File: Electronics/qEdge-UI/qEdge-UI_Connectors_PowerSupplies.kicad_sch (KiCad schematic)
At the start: 29 parts, among them IC201 NCP1117ST33T3G, IC202 AP64501SP-13, J201 Conn_01x02_Male, J202 Conn_01x03_Male

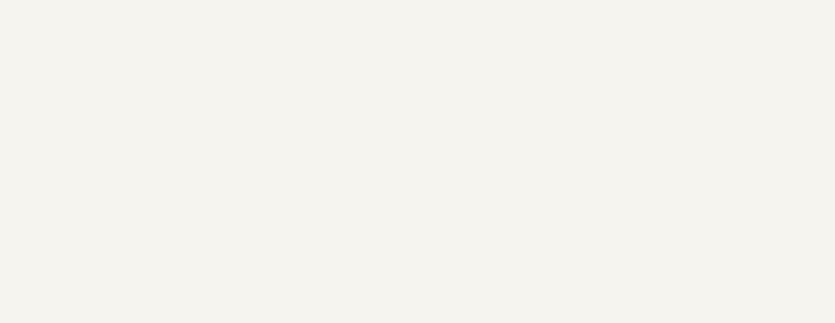
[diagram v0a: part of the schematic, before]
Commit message: added READMEs for Mechanic and Electronic added License in the Electronic schematics restructured Mechanics for better readability and reproducibility
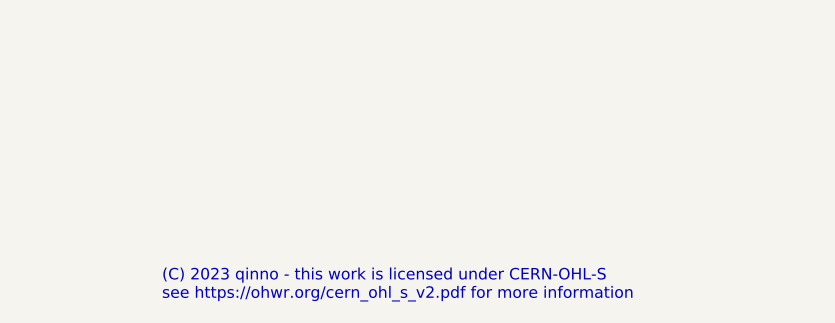
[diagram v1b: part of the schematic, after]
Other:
- note added: "(C) 2023 qinno - this work is licensed under CERN-OHL-S see https://ohwr.org/cern_ohl_s_v2.pdf for more information"
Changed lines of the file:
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@@
+    (effects (font (size 1.27 1.27)) (justify left bottom))
+  )
+  (text "(C) 2023 qinno - this work is licensed under CERN-OHL-S\nsee https://ohwr.org/cern_ohl_s_v2.pdf for more information"
+    (at 237.49 283.21 0)
     (effects (font (size 1.27 1.27)) (justify left bottom))
   )
